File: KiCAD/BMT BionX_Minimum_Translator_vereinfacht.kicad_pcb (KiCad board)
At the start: 2 copper layers, 26 parts, among them J1 Kunteng LCDx Display Connector, J2 SAE Power Connector Motor, J3 Rosenberg Motor, J4 External BB Torquesensor, J5 Brake connector, J6 Throttle connector, J7 CAN Connector, J8 CAN Terminator, Q1 IRF6644, Q2 BCP56, SW1 SW_DPST_x2, U1 BP, U2 MCP2551-CAN Transceiver

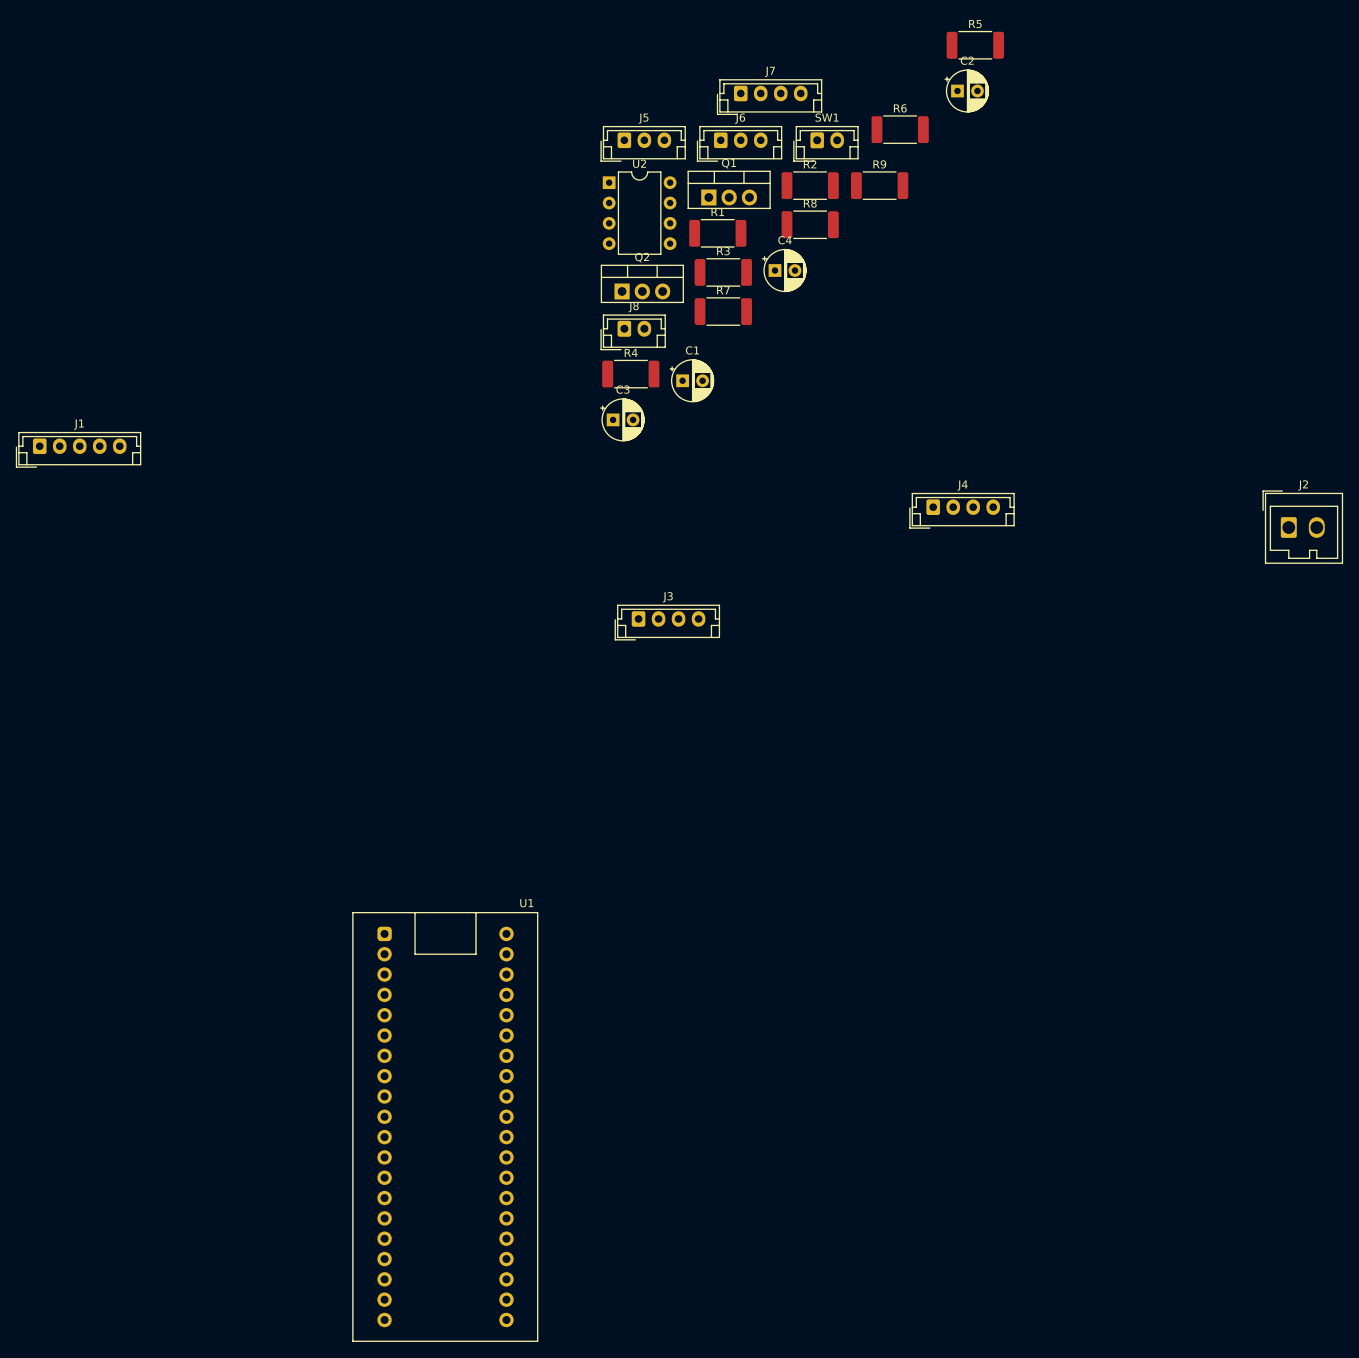
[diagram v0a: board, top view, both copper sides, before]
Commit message: simplified schematic with VOM1271
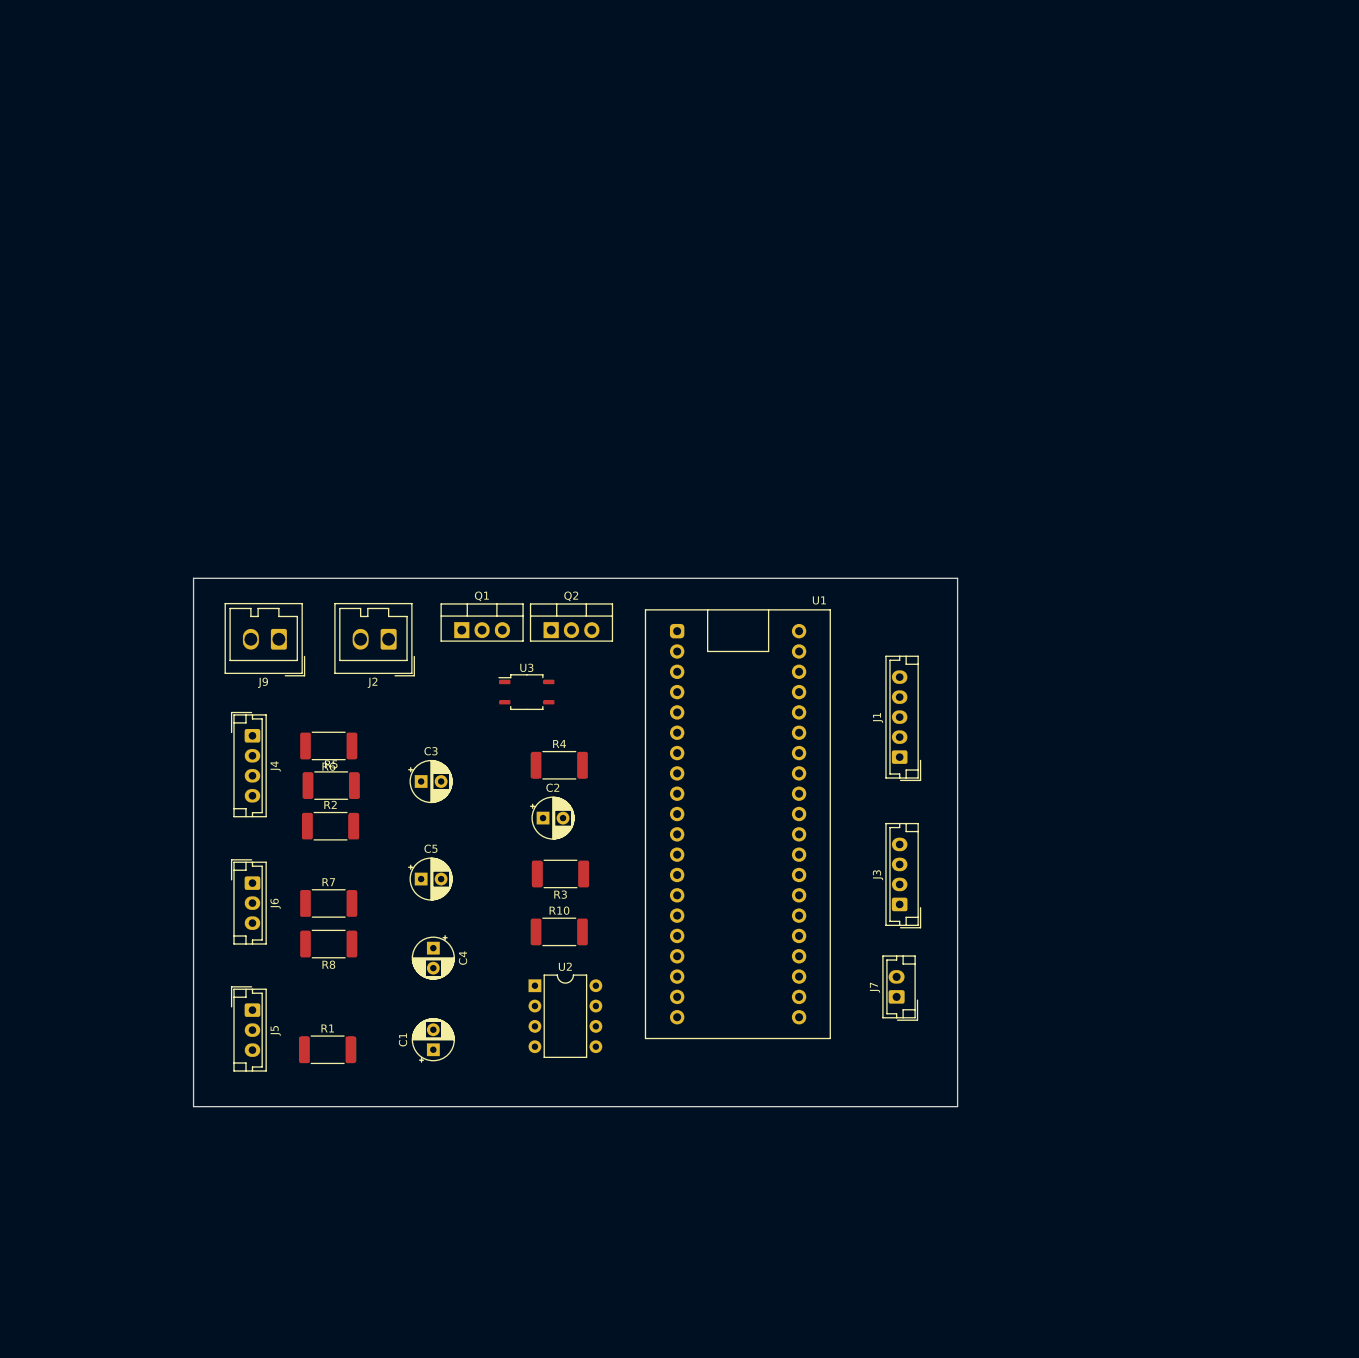
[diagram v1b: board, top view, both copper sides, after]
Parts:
- removed J8: CAN Terminator, Connector_JST:JST_EH_B2B-EH-A_1x02_P2.50mm_Vertical
- removed R9: 120, Resistor_SMD:R_2512_6332Metric
- removed SW1: SW_DPST_x2, Connector_JST:JST_EH_B2B-EH-A_1x02_P2.50mm_Vertical
- added C5: 10µ, Capacitor_THT:CP_Radial_D5.0mm_P2.50mm, F.Cu at (85.9, 98.6)
- added J9: Batterieanschluß, Connector_Wago:Wago_734-132_1x02_P3.50mm_Vertical, F.Cu at (68.1, 68.6)
- added R10: 10k, Resistor_SMD:R_2512_6332Metric, F.Cu at (103.1, 105.2)
- added U3: VOM1271, Package_SO:SOP-4_3.8x4.1mm_P2.54mm, F.Cu at (99.1, 75.2)
- C1: value 47µ -> 10µ
- J7: footprint Connector_JST:JST_EH_B4B-EH-A_1x04_P2.50mm_Vertical -> Connector_JST:JST_EH_B2B-EH-A_1x02_P2.50mm_Vertical
- Q1: value IRF6644 -> IRF3205
- Q2: value BCP56 -> IRF3205
- R1: value 56k -> 2.2k
- R2: value 22k -> 2.2k
- moved R5 122.7 mm to (74.6, 86.9)
- moved J5 118.3 mm to (64.8, 114.9), turned to 270 degrees
- moved J7 114.6 mm to (145.3, 113.3), turned to 90 degrees
- moved J1 114.3 mm to (145.7, 83.3), turned to 90 degrees
- moved J2 113.4 mm to (81.8, 68.6), turned to 180 degrees
- moved R1 113.1 mm to (74.2, 119.9)
- moved J6 109.8 mm to (64.8, 99.1), turned to 270 degrees
- moved R8 108.2 mm to (74.3, 106.7), turned to 180 degrees
- moved R6 105.1 mm to (74.3, 81.9), turned to 180 degrees
- moved C2 104.6 mm to (101.1, 90.9)
- moved U2 100.8 mm to (100.1, 111.9)
- moved R2 100.0 mm to (74.5, 91.9)
- moved C4 94.9 mm to (87.4, 107.2), turned to 270 degrees
- moved J4 89.8 mm to (64.8, 80.6), turned to 270 degrees
- moved C1 89.2 mm to (87.4, 119.9), turned to 90 degrees
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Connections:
- C1 pad 2: -BATT -> GND
- J2 pad 1: +BATT -> Net-(J2-Pad1)
- Q1 pad 1: GND -> Net-(Q1-Pad1)
- Q1 pad 2: Net-(C1-Pad1) -> +BATT
- Q1 pad 3: -BATT -> Net-(Q1-Pad3)
- Q2 pad 1: Net-(C2-Pad1) -> Net-(Q1-Pad1)
- Q2 pad 2: +BATT -> Net-(J2-Pad1)
- Q2 pad 3: Net-(Q2-Pad3) -> Net-(Q1-Pad3)
- R1 pad 1: Net-(R1-Pad1) -> Net-(J5-Pad3)
- R2 pad 1: Net-(C1-Pad1) -> Net-(J4-Pad4)
- R2 pad 2: -BATT -> Net-(C5-Pad1)
- U1 pad PC15: (no net) -> Net-(U1-PadPC15)
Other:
- board outline added: 95.5 x 66 mm
